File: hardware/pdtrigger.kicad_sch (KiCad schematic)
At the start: 85 parts, among them J1 Conn_01x04_Pin, J2 USB_C_Receptacle_USB2.0_16P, J3 Conn_01x02_Pin, Q1 DMP3098LSD-13, Q3 NMOS, SW1 SW_SPDT, SW2 SW_Push, U1 STM32F401RBT6, U2 CYPD3177-24LQXQ, U3 TERM_BLK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

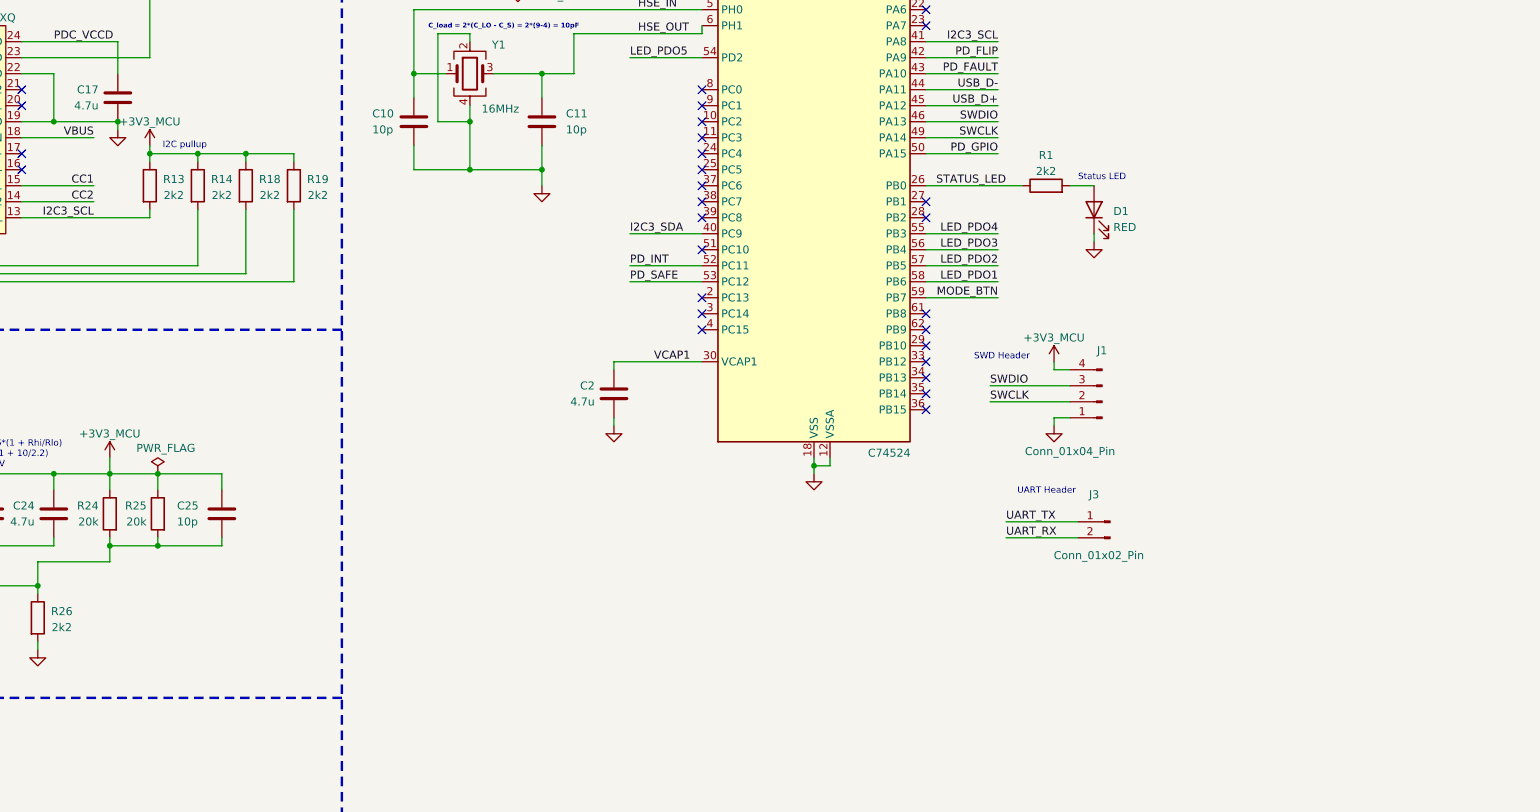
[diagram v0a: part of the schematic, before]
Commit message: firmware work after finally debugging hardware
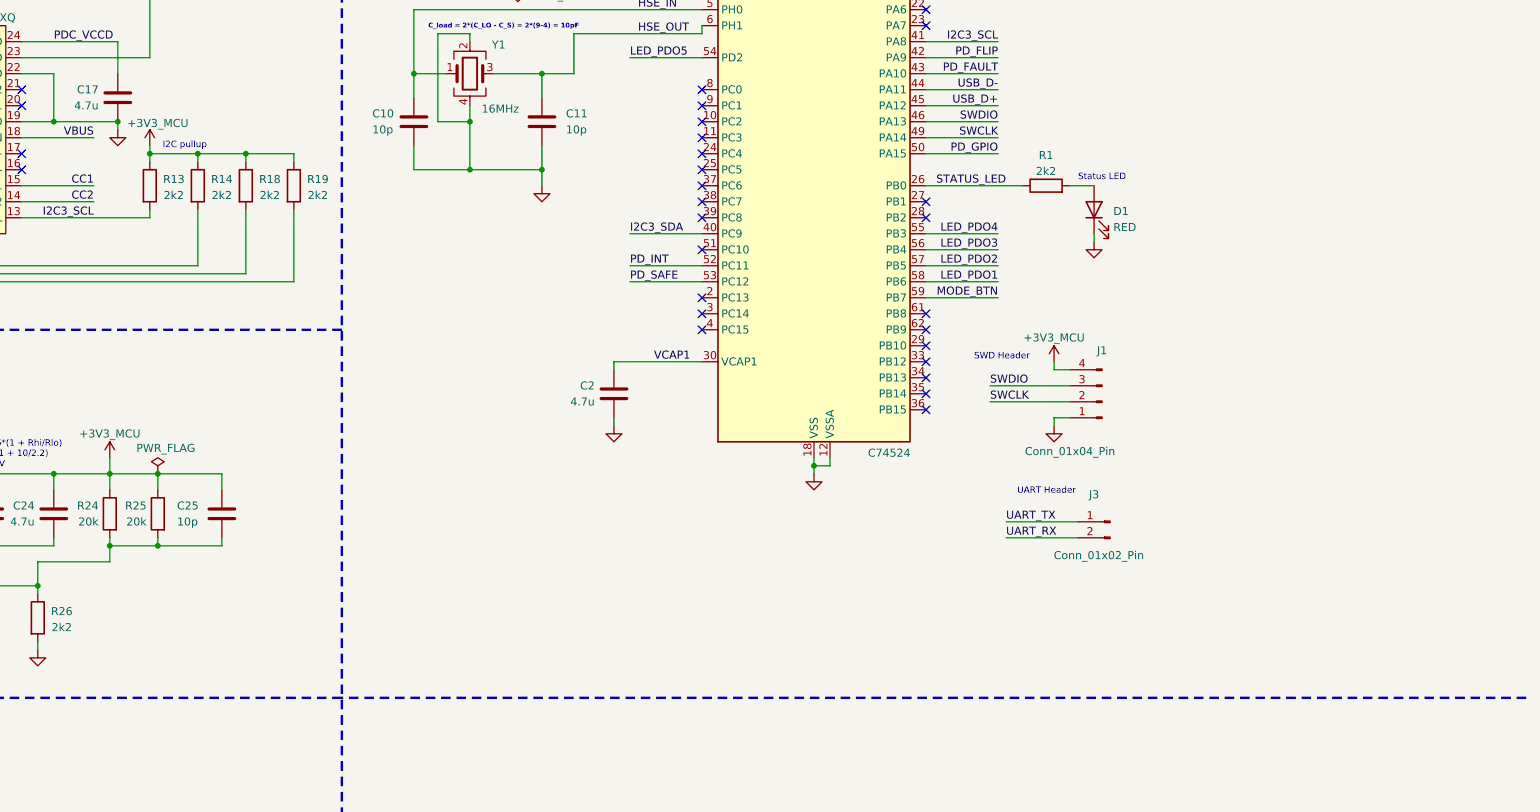
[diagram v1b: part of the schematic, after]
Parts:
- added TP1, TP3: TestPoint, TestPoint:TestPoint_THTPad_D1.5mm_Drill0.7mm, symbol Connector:TestPoint
- renumbered TP3 to TP2
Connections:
- net VBUS: now also TP3.1; no longer TP2.1
- net V_BUS_OUT: now also TP1.1; no longer TP2.1
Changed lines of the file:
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@@
 		)
 	)
+	(polyline
+		(pts
+			(xy 407.67 214.63) (xy 219.71 214.63)
+		)
+		(stroke
+			(width 0.381)
+			(type dash)
+		)
+	)
 	(wire
 		(pts
@@
 		)
 		(property "Value" "+3V3_MCU"
-			(at 189.23 123.19 0)
+			(at 190.5 123.444 0)
 			(effects
 				(font
